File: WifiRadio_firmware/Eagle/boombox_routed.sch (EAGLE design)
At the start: 20 parts, among them J1 POWER_JACKPTH, Y1 16 MHz

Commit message: some small changes
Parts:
- removed C5: 100uF, SparkFun:CAP_POLPTH1
- removed C6: 10uF, SparkFun:CAP_POLPTH2
- removed IC2: (no value), SparkFun:V_REG_78XX-TO-220
- removed J1: POWER_JACKPTH, SparkFun:POWER_JACKPTH
- removed S1: (no value), SparkFun:SWITCH-SPSTPTH
- added PWR: (no value), pinhead:PINHD-1X2
- POT1: value (none) -> 1k
- renumbered SW1 to SW_CONN
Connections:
- removed net 9V: C5.+, IC2.IN, S1.S
- removed net N$26: ATMEGA328.PD7(AIN1), SW_CONN.2
- removed net N$27 (its old number): ATMEGA328.PB0(ICP), SW_CONN.1
- removed net N$28: ATMEGA328.PB1(OC1A), SW_CONN.3
- removed net N$29: ATMEGA328.PB2(SS/OC1B), SW_CONN.5
- removed net N$31: J1.PWR, S1.P
- new net N$19: ATMEGA328.PB0(ICP), SW_CONN.7
- new net N$21: ATMEGA328.PB1(OC1A), SW_CONN.5
- new net N$22: ATMEGA328.PD6(AIN0), SW_CONN.6
- net GND: now also PWR.2, SW_CONN.2; no longer C5.-, C6.-, IC2.GND, J1.GNDBREAK, SW_CONN.7
- net N$23: now also ATMEGA328.PD7(AIN1)
- net N$24: now also SW_CONN.4; no longer SW_CONN.6
- net N$25: now also ATMEGA328.PB2(SS/OC1B), SW_CONN.3; no longer ATMEGA328.PD6(AIN0), SW_CONN.4
- net VCC: now also PWR.1; no longer C6.+, IC2.OUT

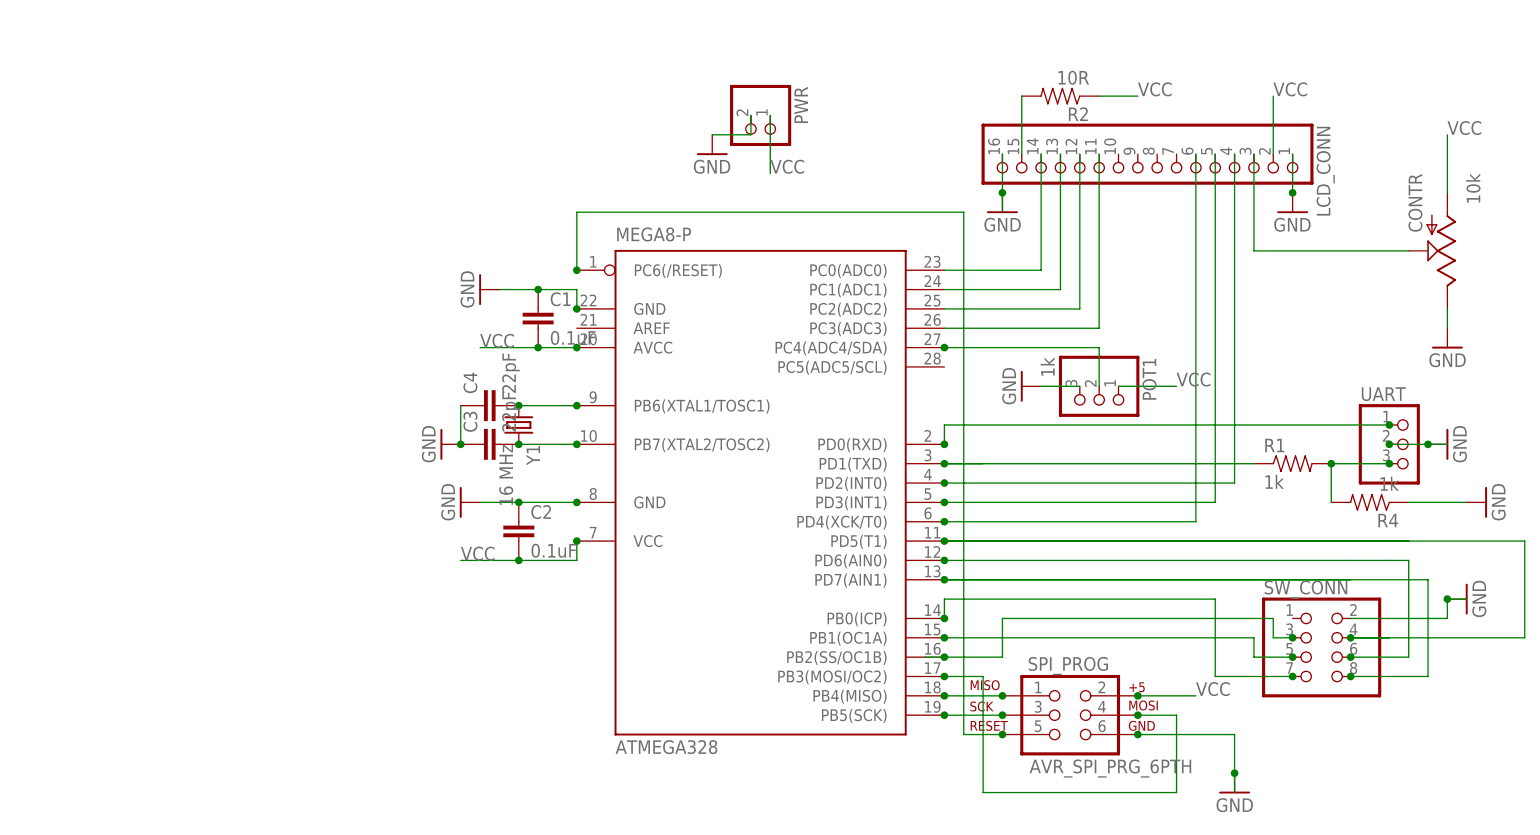
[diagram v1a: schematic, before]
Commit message: Modified boards, changed pin asignment in lcd driver
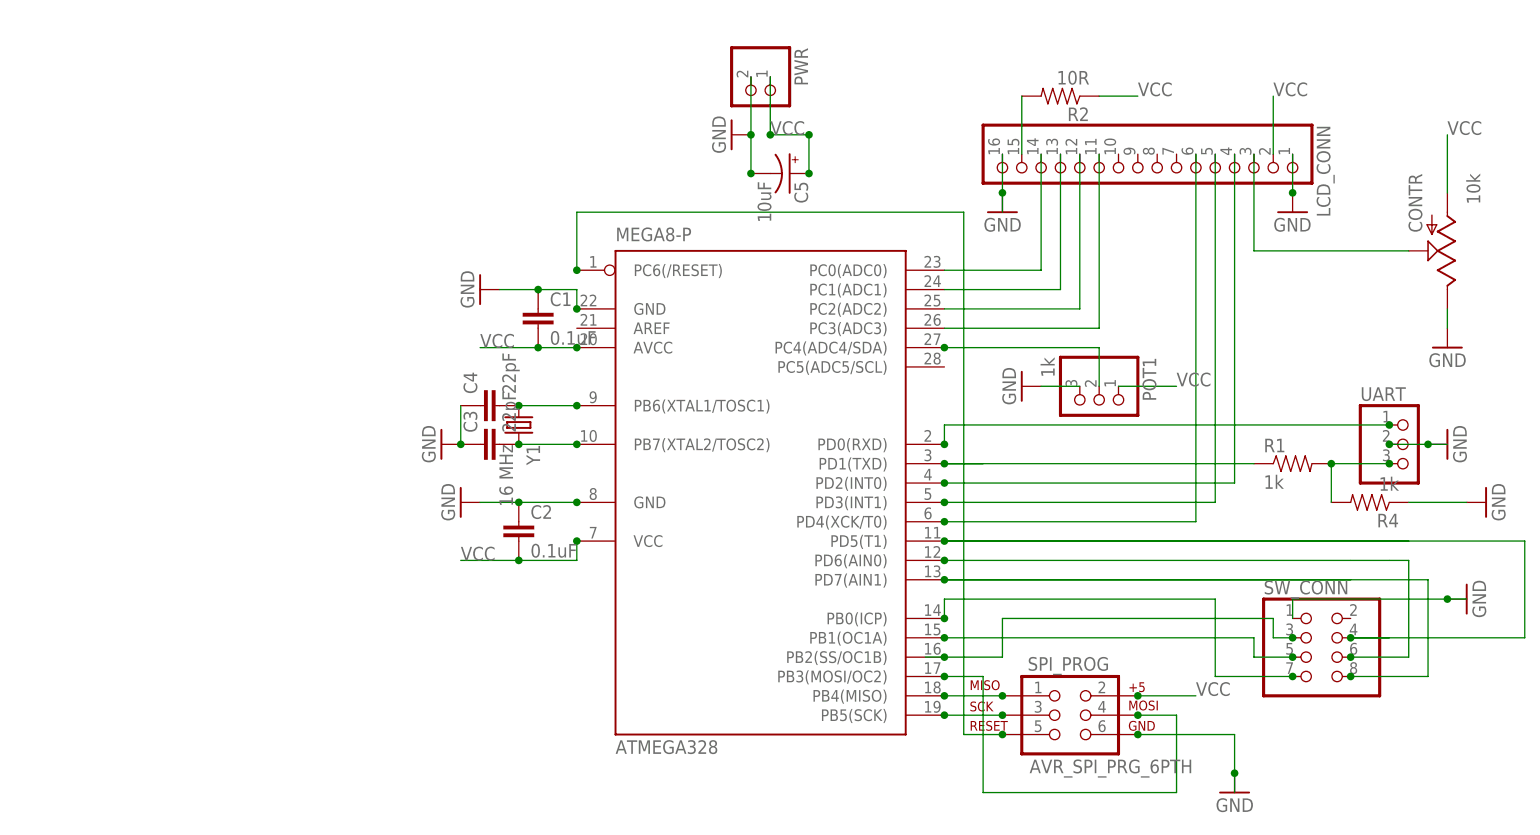
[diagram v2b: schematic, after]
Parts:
- added C5: 10uF, SparkFun:CAP_POLPTH2
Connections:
- net GND: now also C5.-, SW_CONN.1; no longer SW_CONN.2
- net VCC: now also C5.+
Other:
- moved on the sheet: PWR
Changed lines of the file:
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@@
 <part name="GND1" library="SparkFun" deviceset="GND" device=""/>
 <part name="GND2" library="SparkFun" deviceset="GND" device=""/>
+<part name="C5" library="SparkFun" deviceset="CAP_POL" device="PTH2" value="10uF"/>
 </parts>
 <sheets>
@@
 <instance part="POT1" gate="A" x="116.84" y="76.2" rot="R270"/>
 <instance part="GND6" gate="1" x="162.56" y="71.12" rot="MR270"/>
-<instance part="PWR" gate="G$1" x="71.12" y="111.76" rot="R270"/>
-<instance part="GND1" gate="1" x="66.04" y="109.22"/>
+<instance part="PWR" gate="G$1" x="71.12" y="116.84" rot="R270"/>
+<instance part="GND1" gate="1" x="68.58" y="111.76" rot="R270"/>
 <instance part="GND2" gate="1" x="165.1" y="50.8" rot="MR270"/>
+<instance part="C5" gate="G$1" x="76.2" y="106.68" rot="R270"/>
 </instances>
 <busses>
@@
 <segment>
 <pinref part="PWR" gate="G$1" pin="1"/>
-<wire x1="73.66" y1="114.3" x2="73.66" y2="106.68" width="0.1524" layer="91"/>
-<label x="73.66" y="106.68" size="1.778" layer="95"/>
+<wire x1="73.66" y1="119.38" x2="73.66" y2="111.76" width="0.1524" layer="91"/>
+<label x="73.66" y="111.76" size="1.778" layer="95"/>
+<wire x1="73.66" y1="111.76" x2="78.74" y2="111.76" width="0.1524" layer="91"/>
+<pinref part="C5" gate="G$1" pin="+"/>
+<wire x1="78.74" y1="111.76" x2="78.74" y2="106.68" width="0.1524" layer="91"/>
+<junction x="73.66" y="111.76"/>
+<junction x="78.74" y="111.76"/>
+<junction x="78.74" y="106.68"/>
 </segment>
 </net>
@@
 <pinref part="PWR" gate="G$1" pin="2"/>
 <pinref part="GND1" gate="1" pin="GND"/>
-<wire x1="71.12" y1="114.3" x2="71.12" y2="111.76" width="0.1524" layer="91"/>
-<wire x1="71.12" y1="111.76" x2="66.04" y2="111.76" width="0.1524" layer="91"/>
+<wire x1="71.12" y1="119.38" x2="71.12" y2="111.76" width="0.1524" layer="91"/>
+<pinref part="C5" gate="G$1" pin="-"/>
+<wire x1="71.12" y1="111.76" x2="71.12" y2="106.68" width="0.1524" layer="91"/>
+<junction x="71.12" y="111.76"/>
+<junction x="71.12" y="106.68"/>
 </segment>
 <segment>
@@
 <wire x1="162.56" y1="50.8" x2="165.1" y2="50.8" width="0.1524" layer="91"/>
 <junction x="162.56" y="50.8"/>
-<pinref part="SW_CONN" gate="A" pin="2"/>
-<wire x1="149.86" y1="48.26" x2="162.56" y2="48.26" width="0.1524" layer="91"/>
-<wire x1="162.56" y1="48.26" x2="162.56" y2="50.8" width="0.1524" layer="91"/>
+<pinref part="SW_CONN" gate="A" pin="1"/>
+<wire x1="162.56" y1="50.8" x2="142.24" y2="50.8" width="0.1524" layer="91"/>
+<wire x1="142.24" y1="50.8" x2="142.24" y2="48.26" width="0.1524" layer="91"/>
 </segment>
 </net>
